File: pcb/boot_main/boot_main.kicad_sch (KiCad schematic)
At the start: 40 parts, among them J1 Conn_01x10_Pin, P1 USB_C_Plug_USB2.0, SW1 SW_Push, U1 RP2040, U2 NCP1117-3.3_SOT223, U3 W25Q128JVS, U4 AT42QT1070-M, Y1 Crystal_GND24

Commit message: More schematic
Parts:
- added C10, C7: 1u, symbol Device:C
- added C11, C12, C13, C14, C15, C16, C17, C8, C9: 0.1u, symbol Device:C
- added Q1, Q2, Q3: NPN, symbol Simulation_SPICE:NPN
- added R15, R16, R17, R18, R19, R20, R21, R22, R23, R24, R25, R26, R27, R28, R29: R, symbol Device:R
- added R30, R31: 5.1k, symbol Device:R
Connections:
- net +3V3: now also U1.1 (IOVDD), U1.10 (IOVDD), U1.22 (IOVDD), U1.33 (IOVDD), U1.42 (IOVDD), U1.43 (ADC_AVDD), U1.44 (VREG_IN), U1.48 (USB_VDD), U1.49 (IOVDD), C10.1, C11.1, C12.1, C13.1, C14.1, C15.1, C16.1, C17.1, R15.1, R16.1, R17.1, R18.1, R20.1, R21.1, R22.1, R23.1, R26.1, R27.1, R28.1, R29.1
- net GND: now also C10.2, C11.2, C12.2, C13.2, C14.2, C15.2, C16.2, C17.2, C7.2, C8.2, C9.2, Q1.3 (E), Q2.3 (E), Q3.3 (E), R30.2, R31.2
- net at D4.1 (K): now also D1.1 (K), D2.1 (K), D3.1 (K), Q1.1 (C)
- net at D4.2 (A): now also R18.2
- net at D5.1 (K): now also D6.1 (K), D7.1 (K), D8.1 (K), Q2.1 (C)
- net at D5.2 (A): now also R23.2
- net at D8.2 (A): now also R20.2
- net at D3.2 (A): now also R16.2
- net at D12.1 (K): now also D10.1 (K), D11.1 (K), D9.1 (K), Q3.1 (C)
- net at D12.2 (A): now also R29.2
- net at D2.2 (A): now also R15.2
- net at D7.2 (A): now also R21.2
- net at D6.2 (A): now also R22.2
- net B1_LIGHT: now reaches U1.12 (GPIO9)
- net B1_LIGHT: now also R19.1
- net B2_LIGHT: now reaches U1.13 (GPIO10)
- net B2_LIGHT: now also R24.1
- net B3_LIGHT: now reaches U1.14 (GPIO11)
- net B3_LIGHT: now also R25.1
- net SPI_RX: now reaches U1.15 (GPIO12)
- net SPI_CS: now reaches U1.16 (GPIO13)
- net SPI_SCK: now reaches U1.17 (GPIO14)
- net SPI_TX: now reaches U1.18 (GPIO15)
- net +1V1: now reaches U1.23 (DVDD), U1.45 (VREG_VOUT), U1.50 (DVDD)
- net +1V1: now also C7.1, C8.1, C9.1
- net at D9.2 (A): now also R26.2
- net at D10.2 (A): now also R27.2
- net at D11.2 (A): now also R28.2
- net at P1.A5 (CC): now also R31.1
- net at P1.B5 (VCONN): now also R30.1
- net at D1.2 (A): now also R17.2
- new net: Q2.2 (B), R24.2
- new net: Q3.2 (B), R25.2
- new net: Q1.2 (B), R19.2
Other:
- moved on the sheet: C1, C2, C3, C4, D1, D2, D3, D4, D5, D6, D7, D8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

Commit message: More sch, added datasheets
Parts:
- removed C4: 0.1u, symbol Device:C
- removed D1, D10, D11, D12, D2, D3, D4, D5, D6, D7, D8, D9: LED, symbol Device:LED
- removed J1: Conn_01x10_Pin, symbol Connector:Conn_01x10_Pin
- removed Q1, Q2, Q3: NPN, symbol Simulation_SPICE:NPN
- removed R10, R11, R12, R5, R6, R7, R8, R9: 10k, symbol Device:R
- removed R15, R16, R17, R18, R19, R20, R21, R22, R23, R24, R25, R26, R27, R28, R29: R, symbol Device:R
- removed R3, R4: 4.7k, symbol Device:R
- removed U4: AT42QT1070-M, Package_DFN_QFN:VQFN-20-1EP_3x3mm_P0.45mm_EP1.55x1.55mm, symbol Sensor_Touch:AT42QT1070-M
- added J2: Conn_01x02_Pin, symbol Connector:Conn_01x02_Pin
- added R35: 10k, symbol Device:R
- added SW2: SW_Push, symbol Switch:SW_Push
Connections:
- net +3V3: now also U1.26 (RUN), R35.1
- net B1_LIGHT: now also U1.29 (GPIO18); no longer U1.12 (GPIO9)
- net B2_LIGHT: now also U1.31 (GPIO20); no longer U1.13 (GPIO10)
- net B3_LIGHT: now also U1.34 (GPIO22); no longer U1.14 (GPIO11)
- net GND: now also SW2.2
- net SWCLK: now also J2.1 (Pin_1)
- net SWDIO: now also J2.2 (Pin_2)
- new net: R35.2, SW2.1
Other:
- added sheet App Flash (app_flash.kicad_sch)
- added sheet Cap Sense (cap_sense.kicad_sch)
- added sheet LED Ring 1 (led_ring_1.kicad_sch)
- added sheet LED Ring 2 (led_ring_2.kicad_sch)
- added sheet LED Ring 3 (led_ring_3.kicad_sch)
- note added: "Application Blocks"
- note added: "BOOTSEL button forces entry to bootloader by breaking SPI flash communication at boot"
- note added: "Reset mechanism via button"
- moved on the sheet: C10, C11, C12, C13, C14, C15, C16, C17, C5, C6, C7, C8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

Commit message: Assign footprints
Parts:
- C1, C10, C11, C12, C13, C14, C15, C16, C17, C2, C3, C5, C6, C7, C8, C9: footprint (none) -> Capacitor_SMD:C_0603_1608Metric
- J2: footprint (none) -> Connector_PinHeader_2.54mm:PinHeader_1x02_P2.54mm_Vertical
- P1: footprint (none) -> Connector_USB:USB_C_Receptacle_GCT_USB4105-xx-A_16P_TopMnt_Horizontal
- R1, R13, R14, R2, R30, R31, R35: footprint (none) -> Resistor_SMD:R_0603_1608Metric
- SW1, SW2: footprint (none) -> Button_Switch_SMD:SW_Push_1P1T_NO_6x6mm_H9.5mm
- Y1: footprint (none) -> Crystal:Crystal_SMD_3225-4Pin_3.2x2.5mm
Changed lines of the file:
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@@
 			)
 		)
-		(property "Footprint" ""
+		(property "Footprint" "Resistor_SMD:R_0603_1608Metric"
 			(at 55.88 112.268 90)
 			(effects
@@
 			)
 		)
-		(property "Footprint" ""
+		(property "Footprint" "Button_Switch_SMD:SW_Push_1P1T_NO_6x6mm_H9.5mm"
 			(at 179.07 27.94 0)
 			(effects
@@
 			)
 		)
-		(property "Footprint" ""
+		(property "Footprint" "Capacitor_SMD:C_0603_1608Metric"
 			(at 68.2752 165.1 0)
 			(effects
@@
 			)
 		)
-		(property "Footprint" ""
+		(property "Footprint" "Button_Switch_SMD:SW_Push_1P1T_NO_6x6mm_H9.5mm"
 			(at 254 27.94 0)
 			(effects
@@
 			)
 		)
-		(property "Footprint" ""
+		(property "Footprint" "Capacitor_SMD:C_0603_1608Metric"
 			(at 154.6352 64.77 0)
 			(effects
@@
 			)
 		)
-		(property "Footprint" ""
+		(property "Footprint" "Capacitor_SMD:C_0603_1608Metric"
 			(at 200.3552 64.77 0)
 			(effects
@@
 			)
 		)
-		(property "Footprint" ""
+		(property "Footprint" "Capacitor_SMD:C_0603_1608Metric"
 			(at 188.9252 64.77 0)
 			(effects
@@
 			)
 		)
-		(property "Footprint" ""
+		(property "Footprint" "Capacitor_SMD:C_0603_1608Metric"
 			(at 78.4352 33.02 0)
 			(effects
@@
 			)
 		)
-		(property "Footprint" ""
+		(property "Footprint" "Capacitor_SMD:C_0603_1608Metric"
 			(at 117.8052 72.39 0)
 			(effects
@@
 			)
 		)
-		(property "Footprint" ""
+		(property "Footprint" "Capacitor_SMD:C_0603_1608Metric"
 			(at 166.0652 64.77 0)
 			(effects
@@
 			)
 		)
-		(property "Footprint" ""
+		(property "Footprint" "Capacitor_SMD:C_0603_1608Metric"
 			(at 157.1752 81.28 0)
 			(effects
@@
 			)
 		)
-		(property "Footprint" ""
+		(property "Footprint" "Capacitor_SMD:C_0603_1608Metric"
 			(at 107.6452 72.39 0)
 			(effects
@@
 			)
 		)
-		(property "Footprint" ""
+		(property "Footprint" "Resistor_SMD:R_0603_1608Metric"
 			(at 105.41 102.108 90)
 			(effects
@@
 			)
 		)
-		(property "Footprint" ""
+		(property "Footprint" "Capacitor_SMD:C_0603_1608Metric"
 			(at 30.48 109.5248 0)
 			(effects
@@
 			)
 		)
-		(property "Footprint" ""
+		(property "Footprint" "Resistor_SMD:R_0603_1608Metric"
 			(at 56.642 39.37 90)
 			(effects
@@
 			)
 		)
-		(property "Footprint" ""
+		(property "Footprint" "Capacitor_SMD:C_0603_1608Metric"
 			(at 126.6952 81.28 0)
 			(effects
@@
 			)
 		)
-		(property "Footprint" ""
+		(property "Footprint" "Resistor_SMD:R_0603_1608Metric"
 			(at 234.95 34.798 90)
 			(effects
@@
 			)
 		)
-		(property "Footprint" ""
+		(property "Footprint" "Crystal:Crystal_SMD_3225-4Pin_3.2x2.5mm"
 			(at 41.91 106.68 0)
 			(effects
@@
 			)
 		)
-		(property "Footprint" ""
+		(property "Footprint" "Connector_PinHeader_2.54mm:PinHeader_1x02_P2.54mm_Vertical"
 			(at 96.52 161.29 0)
 			(effects
@@
 			)
 		)
-		(property "Footprint" ""
+		(property "Footprint" "Resistor_SMD:R_0603_1608Metric"
 			(at 105.41 109.728 90)
 			(effects
@@
 			)
 		)
-		(property "Footprint" ""
+		(property "Footprint" "Capacitor_SMD:C_0603_1608Metric"
 			(at 223.2152 64.77 0)
 			(effects
@@
 			)
 		)
-		(property "Footprint" ""
+		(property "Footprint" "Capacitor_SMD:C_0603_1608Metric"
 			(at 177.4952 64.77 0)
 			(effects
@@
 			)
 		)
-		(property "Footprint" ""
+		(property "Footprint" "Capacitor_SMD:C_0603_1608Metric"
 			(at 211.7852 64.77 0)
 			(effects
@@
 			)
 		)
-		(property "Footprint" ""
+		(property "Footprint" "Capacitor_SMD:C_0603_1608Metric"
 			(at 106.3752 33.02 0)
 			(effects
@@
 			)
 		)
-		(property "Footprint" ""
+		(property "Footprint" "Resistor_SMD:R_0603_1608Metric"
 			(at 160.02 34.798 90)
 			(effects
@@
 			)
 		)
-		(property "Footprint" ""
+		(property "Footprint" "Capacitor_SMD:C_0603_1608Metric"
 			(at 30.48 101.9048 0)
 			(effects
@@
 			)
 		)
-		(property "Footprint" ""
+		(property "Footprint" "Resistor_SMD:R_0603_1608Metric"
 			(at 66.802 39.37 90)
 			(effects
@@
 			)
 		)
-		(property "Footprint" ""
+		(property "Footprint" "Connector_USB:USB_C_Receptacle_GCT_USB4105-xx-A_16P_TopMnt_Horizontal"
 			(at 33.02 40.64 0)
 			(effects

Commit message: push parts around
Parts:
- C10, C11, C12, C13, C14, C15, C16, C17, C5, C6, C7, C8, C9: footprint Capacitor_SMD:C_0603_1608Metric -> Capacitor_SMD:C_0402_1005Metric
- R1, R14, R2, R30, R31: footprint Resistor_SMD:R_0603_1608Metric -> Resistor_SMD:R_0402_1005Metric
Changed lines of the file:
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@@
 			)
 		)
-		(property "Footprint" "Resistor_SMD:R_0603_1608Metric"
+		(property "Footprint" "Resistor_SMD:R_0402_1005Metric"
 			(at 55.88 112.268 90)
 			(effects
@@
 			)
 		)
-		(property "Footprint" "Capacitor_SMD:C_0603_1608Metric"
+		(property "Footprint" "Capacitor_SMD:C_0402_1005Metric"
 			(at 154.6352 64.77 0)
 			(effects
@@
 			)
 		)
-		(property "Footprint" "Capacitor_SMD:C_0603_1608Metric"
+		(property "Footprint" "Capacitor_SMD:C_0402_1005Metric"
 			(at 200.3552 64.77 0)
 			(effects
@@
 			)
 		)
-		(property "Footprint" "Capacitor_SMD:C_0603_1608Metric"
+		(property "Footprint" "Capacitor_SMD:C_0402_1005Metric"
 			(at 188.9252 64.77 0)
 			(effects
@@
 			)
 		)
-		(property "Footprint" "Capacitor_SMD:C_0603_1608Metric"
+		(property "Footprint" "Capacitor_SMD:C_0402_1005Metric"
 			(at 117.8052 72.39 0)
 			(effects
@@
 			)
 		)
-		(property "Footprint" "Capacitor_SMD:C_0603_1608Metric"
+		(property "Footprint" "Capacitor_SMD:C_0402_1005Metric"
 			(at 166.0652 64.77 0)
 			(effects
@@
 			)
 		)
-		(property "Footprint" "Capacitor_SMD:C_0603_1608Metric"
+		(property "Footprint" "Capacitor_SMD:C_0402_1005Metric"
 			(at 157.1752 81.28 0)
 			(effects
@@
 			)
 		)
-		(property "Footprint" "Capacitor_SMD:C_0603_1608Metric"
+		(property "Footprint" "Capacitor_SMD:C_0402_1005Metric"
 			(at 107.6452 72.39 0)
 			(effects
@@
 			)
 		)
-		(property "Footprint" "Resistor_SMD:R_0603_1608Metric"
+		(property "Footprint" "Resistor_SMD:R_0402_1005Metric"
 			(at 105.41 102.108 90)
 			(effects
@@
 			)
 		)
-		(property "Footprint" "Capacitor_SMD:C_0603_1608Metric"
+		(property "Footprint" "Capacitor_SMD:C_0402_1005Metric"
 			(at 30.48 109.5248 0)
 			(effects
@@
 			)
 		)
-		(property "Footprint" "Resistor_SMD:R_0603_1608Metric"
+		(property "Footprint" "Resistor_SMD:R_0402_1005Metric"
 			(at 56.642 39.37 90)
 			(effects
@@
 			)
 		)
-		(property "Footprint" "Capacitor_SMD:C_0603_1608Metric"
+		(property "Footprint" "Capacitor_SMD:C_0402_1005Metric"
 			(at 126.6952 81.28 0)
 			(effects
@@
 			)
 		)
-		(property "Footprint" "Resistor_SMD:R_0603_1608Metric"
+		(property "Footprint" "Resistor_SMD:R_0402_1005Metric"
 			(at 105.41 109.728 90)
 			(effects
@@
 			)
 		)
-		(property "Footprint" "Capacitor_SMD:C_0603_1608Metric"
+		(property "Footprint" "Capacitor_SMD:C_0402_1005Metric"
 			(at 223.2152 64.77 0)
 			(effects
@@
 			)
 		)
-		(property "Footprint" "Capacitor_SMD:C_0603_1608Metric"
+		(property "Footprint" "Capacitor_SMD:C_0402_1005Metric"
 			(at 177.4952 64.77 0)
 			(effects
@@
 			)
 		)
-		(property "Footprint" "Capacitor_SMD:C_0603_1608Metric"
+		(property "Footprint" "Capacitor_SMD:C_0402_1005Metric"
 			(at 211.7852 64.77 0)
 			(effects
@@
 			)
 		)
-		(property "Footprint" "Capacitor_SMD:C_0603_1608Metric"
+		(property "Footprint" "Capacitor_SMD:C_0402_1005Metric"
 			(at 30.48 101.9048 0)
 			(effects
@@
 			)
 		)
-		(property "Footprint" "Resistor_SMD:R_0603_1608Metric"
+		(property "Footprint" "Resistor_SMD:R_0402_1005Metric"
 			(at 66.802 39.37 90)
 			(effects

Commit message: Some initial layout
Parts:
- removed U3: W25Q128JVS, Package_SO:SOIC-8_5.23x5.23mm_P1.27mm, symbol Memory_Flash:W25Q128JVS
- added U3: W25Q32JVZP, Package_SON:WSON-8-1EP_6x5mm_P1.27mm_EP3.4x4.3mm, symbol Memory_Flash:W25Q32JVZP
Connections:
- net +3V3: now also U3.8 (VCC)
- net CAP_CHG: now also U1.4 (GPIO2); no longer U1.9 (GPIO7)
- net CAP_RES: now also U1.5 (GPIO3); no longer U1.8 (GPIO6)
- net GND: now also U3.4 (GND), U3.9 (EP)
- net QSPI_SCLK: now also U3.6 (CLK)
- net QSPI_SD0: now also U3.5 (DI(IO0))
- net QSPI_SD1: now also U3.2 (DO(IO1))
- net QSPI_SD2: now also U3.3 (IO2)
- net QSPI_SD3: now also U3.7 (IO3)
- net QSPI_SS: now also U3.1 (~{CS})
- net SCL: now also U1.3 (GPIO1); no longer U1.7 (GPIO5)
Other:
- note added: "Place near pin 44"
- note added: "Place near pin 45"
- note added: "TODO: Maybe change from buttons to pins?"
- note added: "TODO: Verify GND connection"
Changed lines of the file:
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@@
 	)
 	(junction
+		(at 52.07 187.96)
+		(diameter 0)
+		(color 0 0 0 0)
+	)
+	(junction
 		(at 165.1 57.15)
 		(diameter 0)
@@
 	(wire
 		(pts
-			(xy 163.83 107.95) (xy 173.99 107.95)
+			(xy 163.83 97.79) (xy 173.99 97.79)
 		)
 		(stroke
@@
 	(wire
 		(pts
-			(xy 52.07 186.69) (xy 52.07 189.23)
+			(xy 52.07 186.69) (xy 52.07 187.96)
 		)
 		(stroke
@@
 	(wire
 		(pts
+			(xy 54.61 187.96) (xy 52.07 187.96)
+		)
+		(stroke
+			(width 0)
+			(type default)
+		)
+	)
+	(wire
+		(pts
 			(xy 210.82 67.31) (xy 222.25 67.31)
 		)
@@
 	(wire
 		(pts
+			(xy 54.61 186.69) (xy 54.61 187.96)
+		)
+		(stroke
+			(width 0)
+			(type default)
+		)
+	)
+	(wire
+		(pts
 			(xy 52.07 152.4) (xy 52.07 154.94)
 		)
@@
 	(wire
 		(pts
-			(xy 163.83 110.49) (xy 173.99 110.49)
+			(xy 163.83 102.87) (xy 173.99 102.87)
 		)
 		(stroke
@@
 	(wire
 		(pts
-			(xy 163.83 113.03) (xy 173.99 113.03)
+			(xy 163.83 100.33) (xy 173.99 100.33)
 		)
 		(stroke
@@
 	(wire
 		(pts
+			(xy 52.07 187.96) (xy 52.07 189.23)
+		)
+		(stroke
+			(width 0)
+			(type default)
+		)
+	)
+	(wire
+		(pts
 			(xy 104.14 113.03) (xy 113.03 113.03)
 		)
@@
 		)
 	)
+	(rectangle
+		(start 49.53 179.07)
+		(end 72.39 195.58)
+		(stroke
+			(width 0)
+			(type default)
+		)
+		(fill
+			(type none)
+		)
+	)
+	(rectangle
+		(start 138.43 15.24)
+		(end 269.24 44.45)
+		(stroke
+			(width 0)
+			(type default)
+		)
+		(fill
+			(type none)
+		)
+	)
 	(text "BOOTSEL button forces entry to bootloader\nby breaking SPI flash communication at boot"
 		(exclude_from_sim no)
@@
 		)
 	)
+	(text "TODO: Verify GND \nconnection"
+		(exclude_from_sim no)
+		(at 62.992 191.77 0)
+		(effects
+			(font
+				(size 1.27 1.27)
+			)
+		)
+	)
+	(text "Place near pin 44"
+		(exclude_from_sim no)
+		(at 166.37 81.788 0)
+		(effects
+			(font
+				(size 1.27 1.27)
+			)
+		)
+	)
+	(text "Place near \npin 45"
+		(exclude_from_sim no)
+		(at 120.65 81.534 0)
+		(effects
+			(font
+				(size 1.27 1.27)
+			)
+		)
+	)
 	(text "Reset mechanism via button"
 		(exclude_from_sim no)
@@
 		)
 	)
+	(text "TODO: Maybe change from \nbuttons to pins?"
+		(exclude_from_sim no)
+		(at 206.248 27.94 0)
+		(effects
+			(font
+				(size 1.27 1.27)
+			)
+		)
+	)
 	(label "B2_LIGHT"
 		(at 165.1 146.05 0)
@@
 	)
 	(label "CAP_CHG"
-		(at 165.1 113.03 0)
+		(at 165.1 100.33 0)
 		(fields_autoplaced yes)
 		(effects
@@
 	)
 	(label "CAP_RES"
-		(at 165.1 110.49 0)
+		(at 165.1 102.87 0)
 		(fields_autoplaced yes)
 		(effects
@@
 	)
 	(label "SCL"
-		(at 170.18 107.95 0)
+		(at 170.18 97.79 0)
 		(fields_autoplaced yes)
 		(effects
@@
 	)
 	(symbol
-		(lib_id "Memory_Flash:W25Q128JVS")
-		(at 52.07 173.99 0)
-		(unit 1)
-		(exclude_from_sim no)
-		(in_bom yes)
-		(on_board yes)
-		(dnp no)
-		(fields_autoplaced yes)
-		(property "Reference" "U3"
-			(at 60.96 172.7199 0)
-			(effects
-				(font
-					(size 1.27 1.27)
-				)
-				(justify left)
-			)
-		)
-		(property "Value" "W25Q128JVS"
-			(at 60.96 175.2599 0)
-			(effects
-				(font
-					(size 1.27 1.27)
-				)
-				(justify left)
-			)
-		)
-		(property "Footprint" "Package_SO:SOIC-8_5.23x5.23mm_P1.27mm"
-			(at 52.07 173.99 0)
-			(effects
-				(font
-					(size 1.27 1.27)
-				)
-				(hide yes)
-			)
-		)
-		(property "Datasheet" "http://www.winbond.com/resource-files/w25q128jv_dtr%20revc%2003272018%20plus.pdf"
-			(at 52.07 173.99 0)
-			(effects
-				(font
-					(size 1.27 1.27)
-				)
-				(hide yes)
-			)
-		)
-		(property "Description" "128Mb Serial Flash Memory, Standard/Dual/Quad SPI, SOIC-8"
-			(at 52.07 173.99 0)
-			(effects
-				(font
-					(size 1.27 1.27)
-				)
-				(hide yes)
-			)
-		)
-		(pin "5"
-		)
-		(pin "7"
-		)
-		(pin "6"
-		)
-		(pin "8"
-		)
-		(pin "2"
-		)
-		(pin "1"
-		)
-		(pin "4"
-		)
-		(pin "3"
-		)
-		(instances
-			(project "boot_main"
-				(path "/ed98915d-12a7-4f29-9c7c-423444196a5a"
-					(reference "U3")
-					(unit 1)
-				)
-			)
-		)
-	)
-	(symbol
 		(lib_id "power:GND")
 		(at 106.68 77.47 0)
@@
 					(unit 1)
 				)
+			)
+		)
+	)
+	(symbol
+		(lib_id "Memory_Flash:W25Q32JVZP")
+		(at 52.07 173.99 0)
+		(unit 1)
+		(exclude_from_sim no)
+		(in_bom yes)
+		(on_board yes)
+		(dnp no)
+		(fields_autoplaced yes)
+		(property "Reference" "U3"
+			(at 60.96 172.7199 0)
+			(effects
+				(font
+					(size 1.27 1.27)
+				)
+				(justify left)
+			)
+		)
+		(property "Value" "W25Q32JVZP"
+			(at 60.96 175.2599 0)
+			(effects
+				(font
+					(size 1.27 1.27)
+				)
+				(justify left)
+			)
+		)
+		(property "Footprint" "Package_SON:WSON-8-1EP_6x5mm_P1.27mm_EP3.4x4.3mm"
+			(at 52.07 173.99 0)
+			(effects
+				(font
+					(size 1.27 1.27)
+				)
+				(hide yes)
+			)
+		)
+		(property "Datasheet" "http://www.winbond.com/resource-files/w25q32jv%20revg%2003272018%20plus.pdf"
+			(at 52.07 176.53 0)
+			(effects
+				(font
+					(size 1.27 1.27)
+				)
+				(hide yes)
+			)
+		)
+		(property "Description" "32Mb Serial Flash Memory, Standard/Dual/Quad SPI, DFN-8"
+			(at 52.07 173.99 0)
+			(effects
+				(font
+					(size 1.27 1.27)
+				)
+				(hide yes)
+			)
+		)
+		(pin "8"
+		)
+		(pin "4"
+		)
+		(pin "2"
+		)
+		(pin "3"
+		)
+		(pin "1"
+		)
+		(pin "9"
+		)
+		(pin "7"
+		)
+		(pin "6"
+		)
+		(pin "5"
+		)
+		(instances
+			(project ""
+				(path "/ed98915d-12a7-4f29-9c7c-423444196a5a"
+					(reference "U3")
+					(unit 1)
+				)

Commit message: MOre layout
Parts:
- added H1, H2, H3, H4: MountingHole, MountingHole:MountingHole_3.2mm_M3, symbol Mechanical:MountingHole
- P1: footprint Connector_USB:USB_C_Receptacle_GCT_USB4105-xx-A_16P_TopMnt_Horizontal -> Connector_USB:USB_C_Receptacle_GCT_USB4115-03-C

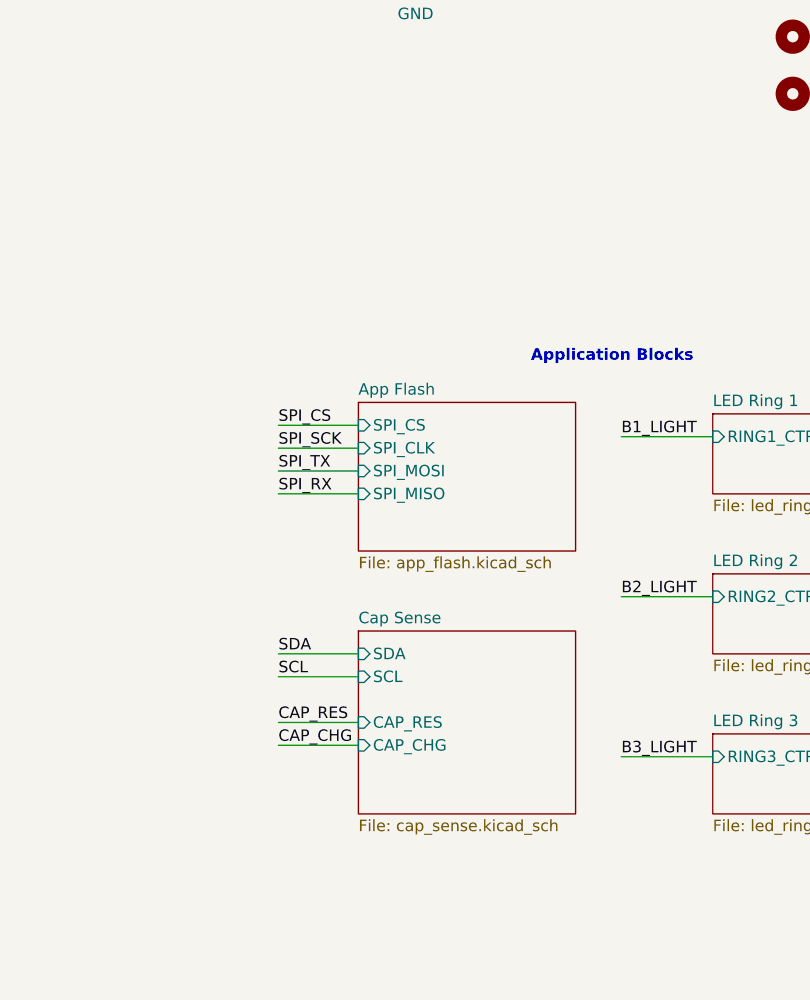
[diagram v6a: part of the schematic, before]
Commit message: move cap sense ic to front panel
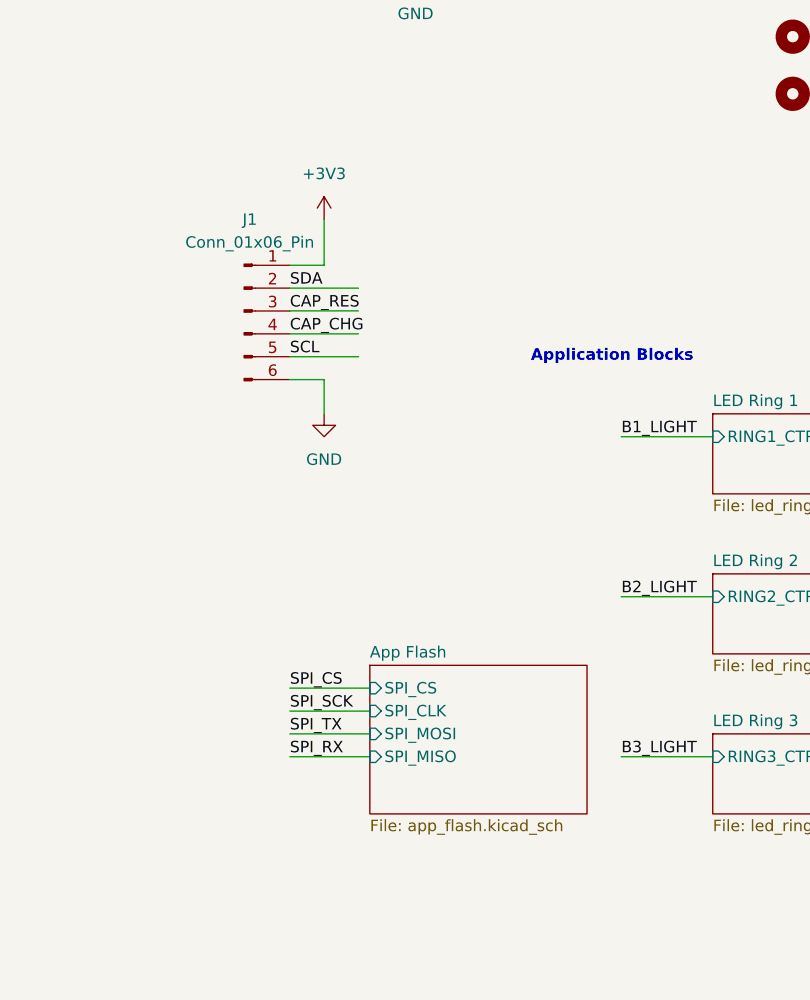
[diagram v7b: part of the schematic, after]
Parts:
- added J1: Conn_01x06_Pin, Connector_FFC-FPC:Hirose_FH12-6S-0.5SH_1x06-1MP_P0.50mm_Horizontal, symbol Connector:Conn_01x06_Pin
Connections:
- net +3V3: now also J1.1 (Pin_1)
- net CAP_CHG: now also J1.4 (Pin_4)
- net CAP_RES: now also J1.3 (Pin_3)
- net GND: now also J1.6 (Pin_6)
- net SCL: now also J1.5 (Pin_5)
- net SDA: now also J1.2 (Pin_2)
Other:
- removed sheet Cap Sense
